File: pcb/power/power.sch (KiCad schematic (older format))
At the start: 28 parts, among them J1 Conn_Coaxial_Power, J2 GS3, SW1 SW_SPST, U1 L7805

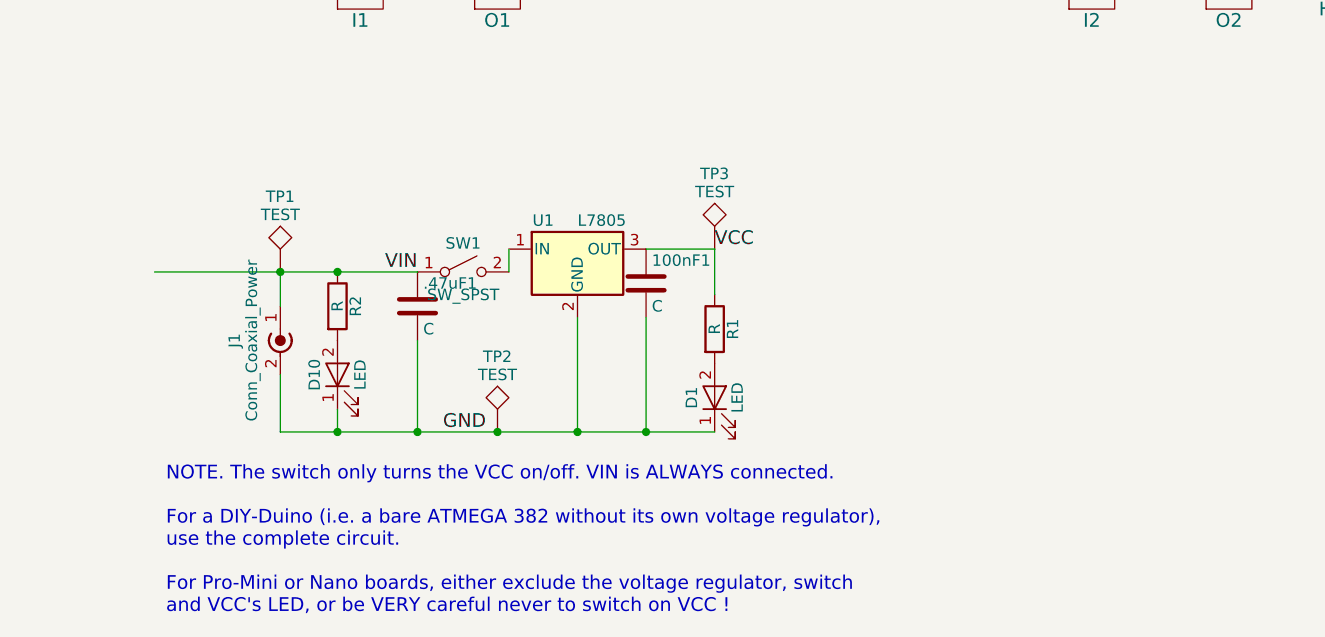
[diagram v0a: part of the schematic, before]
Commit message: Tidied up blank, and removed the voltage regulator from "power" module.
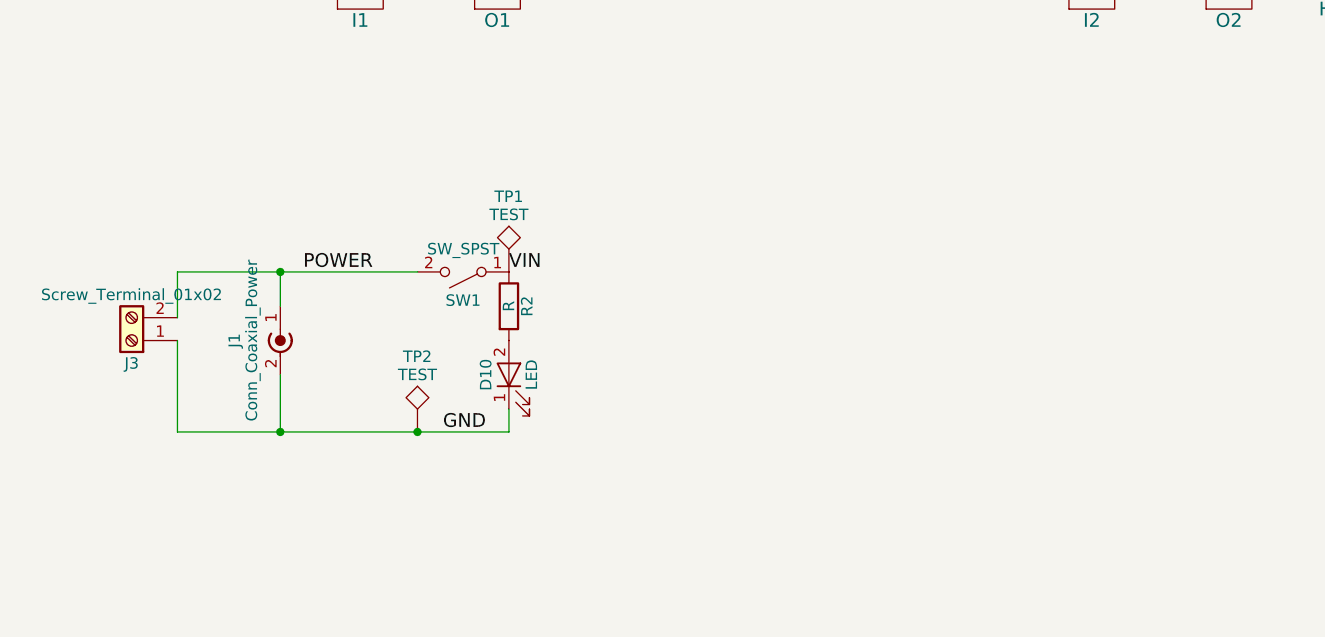
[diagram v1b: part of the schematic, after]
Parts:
- removed .47uF1, 100nF1: C, Capacitors_THT:CP_Radial_D6.3mm_P2.50mm, symbol C
- removed D1: LED, LEDs:LED_D3.0mm, symbol LED
- removed R1: R, Resistors_THT:R_Axial_DIN0204_L3.6mm_D1.6mm_P7.62mm_Horizontal, symbol R
- removed TP3: TEST, Connectors:PINTST, symbol TEST
- removed U1: L7805, Power_Integrations:TO-220, symbol L7805
- added J3: Screw_Terminal_01x02, Connectors_Terminal_Blocks:TerminalBlock_Philmore_TB132_02x5mm_Straight, symbol Screw_Terminal_01x02
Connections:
- net Earth: now also J3.1 (Pin_1)
- net VIN: no longer J1.1 (In)
- net POWER: now reaches SW1.2 (B)
- net POWER: now also J1.1 (In), J3.2 (Pin_2)
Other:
- note removed: "NOTE. The switch only turns the VCC on/off. VIN is ALWAYS connected.\n\nFor a DIY-Duino (i.e. a bare ATMEGA 382 without its own voltage regulator),\nuse the complete circuit.\n\nFor Pro-Mini or Nano boards, either exclude the voltage regulator, switch\nand VCC's LED, or be VERY careful never to switch on VCC !"
- moved on the sheet: D10, R2, SW1, TP1, TP2
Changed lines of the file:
@@
 	1    0    0    -1
 $EndComp
-$Comp
-L L7805 U1
-U 1 1 5AC3DA6D
-P 3050 4000
-F 0 "U1" H 2900 4125 50  0000 C CNN
-F 1 "L7805" H 3050 4125 50  0000 L CNN
-F 2 "Power_Integrations:TO-220" H 3075 3850 50  0001 L CIN
-F 3 "" H 3050 3950 50  0001 C CNN
-	1    3050 4000
-	1    0    0    -1
-$EndComp
-$Comp
-L C .47uF1
-U 1 1 5AC3DA90
-P 2350 4250
-F 0 ".47uF1" H 2375 4350 50  0000 L CNN
-F 1 "C" H 2375 4150 50  0000 L CNN
-F 2 "Capacitors_THT:CP_Radial_D6.3mm_P2.50mm" H 2388 4100 50  0001 C CNN
-F 3 "" H 2350 4250 50  0001 C CNN
-	1    2350 4250
-	1    0    0    -1
-$EndComp
-$Comp
-L C 100nF1
-U 1 1 5AC3DAAD
-P 3350 4150
-F 0 "100nF1" H 3375 4250 50  0000 L CNN
-F 1 "C" H 3375 4050 50  0000 L CNN
-F 2 "Capacitors_THT:CP_Radial_D6.3mm_P2.50mm" H 3388 4000 50  0001 C CNN
-F 3 "" H 3350 4150 50  0001 C CNN
-	1    3350 4150
-	1    0    0    -1
-$EndComp
-$Comp
-L R R1
-U 1 1 5AC3DACC
-P 3650 4350
-F 0 "R1" V 3730 4350 50  0000 C CNN
-F 1 "R" V 3650 4350 50  0000 C CNN
-F 2 "Resistors_THT:R_Axial_DIN0204_L3.6mm_D1.6mm_P7.62mm_Horizontal" V 3580 4350 50  0001 C CNN
-F 3 "" H 3650 4350 50  0001 C CNN
-	1    3650 4350
-	1    0    0    -1
-$EndComp
-$Comp
-L LED D1
-U 1 1 5AC3DC09
-P 3650 4650
-F 0 "D1" H 3650 4750 50  0000 C CNN
-F 1 "LED" H 3650 4550 50  0000 C CNN
-F 2 "LEDs:LED_D3.0mm" H 3650 4650 50  0001 C CNN
-F 3 "" H 3650 4650 50  0001 C CNN
-	1    3650 4650
-	0    -1   -1   0
-$EndComp
-Text Label 2350 4100 2    60   ~ 0
+Text Label 2750 4100 0    60   ~ 0
 VIN
-Text Label 3650 4000 0    60   ~ 0
-VCC
 $Comp
 L Conn_Coaxial_Power J1
@@
 L R R2
 U 1 1 5AC48099
-P 2000 4250
-F 0 "R2" V 2080 4250 50  0000 C CNN
-F 1 "R" V 2000 4250 50  0000 C CNN
-F 2 "Resistors_THT:R_Axial_DIN0204_L3.6mm_D1.6mm_P7.62mm_Horizontal" V 1930 4250 50  0001 C CNN
-F 3 "" H 2000 4250 50  0001 C CNN
-	1    2000 4250
+P 2750 4250
+F 0 "R2" V 2830 4250 50  0000 C CNN
+F 1 "R" V 2750 4250 50  0000 C CNN
+F 2 "Resistors_THT:R_Axial_DIN0204_L3.6mm_D1.6mm_P7.62mm_Horizontal" V 2680 4250 50  0001 C CNN
+F 3 "" H 2750 4250 50  0001 C CNN
+	1    2750 4250
 	1    0    0    -1
 $EndComp
@@
 L LED D10
 U 1 1 5AC480E4
-P 2000 4550
-F 0 "D10" H 2000 4650 50  0000 C CNN
-F 1 "LED" H 2000 4450 50  0000 C CNN
-F 2 "LEDs:LED_D3.0mm" H 2000 4550 50  0001 C CNN
-F 3 "" H 2000 4550 50  0001 C CNN
-	1    2000 4550
+P 2750 4550
+F 0 "D10" H 2750 4650 50  0000 C CNN
+F 1 "LED" H 2750 4450 50  0000 C CNN
+F 2 "LEDs:LED_D3.0mm" H 2750 4550 50  0001 C CNN
+F 3 "" H 2750 4550 50  0001 C CNN
+	1    2750 4550
 	0    -1   -1   0
 $EndComp
@@
 F 3 "" H 2550 4100 50  0001 C CNN
 	1    2550 4100
-	1    0    0    -1
+	-1   0    0    1
 $EndComp
 $Comp
 L TEST TP1
 U 1 1 5AC4A364
-P 1750 4100
-F 0 "TP1" H 1750 4400 50  0000 C BNN
-F 1 "TEST" H 1750 4350 50  0000 C CNN
-F 2 "Connectors:PINTST" H 1750 4100 50  0001 C CNN
-F 3 "" H 1750 4100 50  0001 C CNN
-	1    1750 4100
-	1    0    0    -1
-$EndComp
-$Comp
-L TEST TP3
-U 1 1 5AC4A405
-P 3650 4000
-F 0 "TP3" H 3650 4300 50  0000 C BNN
-F 1 "TEST" H 3650 4250 50  0000 C CNN
-F 2 "Connectors:PINTST" H 3650 4000 50  0001 C CNN
-F 3 "" H 3650 4000 50  0001 C CNN
-	1    3650 4000
+P 2750 4100
+F 0 "TP1" H 2750 4400 50  0000 C BNN
+F 1 "TEST" H 2750 4350 50  0000 C CNN
+F 2 "Connectors:PINTST" H 2750 4100 50  0001 C CNN
+F 3 "" H 2750 4100 50  0001 C CNN
+	1    2750 4100
 	1    0    0    -1
 $EndComp
@@
 L TEST TP2
 U 1 1 5AC4A450
-P 2700 4800
-F 0 "TP2" H 2700 5100 50  0000 C BNN
-F 1 "TEST" H 2700 5050 50  0000 C CNN
-F 2 "Connectors:PINTST" H 2700 4800 50  0001 C CNN
-F 3 "" H 2700 4800 50  0001 C CNN
-	1    2700 4800
+P 2350 4800
+F 0 "TP2" H 2350 5100 50  0000 C BNN
+F 1 "TEST" H 2350 5050 50  0000 C CNN
+F 2 "Connectors:PINTST" H 2350 4800 50  0001 C CNN
+F 3 "" H 2350 4800 50  0001 C CNN
+	1    2350 4800
 	1    0    0    -1
 $EndComp
@@
 Text Notes 6450 1850 0    60   ~ 0
 Use jumpers to enable each LED.
-Text Notes 1250 5600 0    60   ~ 0
-NOTE. The switch only turns the VCC on/off. VIN is ALWAYS connected.\n\nFor a DIY-Duino (i.e. a bare ATMEGA 382 without its own voltage regulator),\nuse the complete circuit.\n\nFor Pro-Mini or Nano boards, either exclude the voltage regulator, switch\nand VCC's LED, or be VERY careful never to switch on VCC !
-Wire Wire Line
-	2350 4400 2350 4800
 Wire Wire Line
 	6850 2150 7400 2150
@@
 Wire Wire Line
 	8000 3600 7700 3600
-Connection ~ 2000 4100
 Wire Wire Line
 	1750 4250 1750 4100
-Connection ~ 1750 4100
 Wire Wire Line
 	1750 4550 1750 4800
-Wire Wire Line
-	1200 4100 2350 4100
-Wire Wire Line
-	2000 4800 2000 4700
 Connection ~ 2350 4800
-Connection ~ 2000 4800
-Wire Wire Line
-	1750 4800 3650 4800
-Wire Wire Line
-	3350 4800 3350 4300
-Connection ~ 3350 4800
-Wire Wire Line
-	3650 4200 3650 4000
-Wire Wire Line
-	3650 4000 3350 4000
-Wire Wire Line
-	3050 4300 3050 4800
-Connection ~ 3050 4800
-Wire Wire Line
-	2750 4100 2750 4000
-Connection ~ 2700 4800
 $Comp
 L Output O2
@@
 Wire Wire Line
 	5600 2150 6050 2150
+Wire Wire Line
+	1300 4800 2750 4800
+Wire Wire Line
+	2750 4800 2750 4700
+Wire Wire Line
+	1300 4100 2350 4100
+Text Label 1850 4100 0    60   ~ 0
+POWER
+$Comp
+L Screw_Terminal_01x02 J3
+U 1 1 5AC4EAFB
+P 1100 4400
+F 0 "J3" H 1100 4500 50  0000 C CNN
+F 1 "Screw_Terminal_01x02" H 1100 4200 50  0000 C CNN
+F 2 "Connectors_Terminal_Blocks:TerminalBlock_Philmore_TB132_02x5mm_Straight" H 1100 4400 50  0001 C CNN
+F 3 "" H 1100 4400 50  0001 C CNN
+	1    1100 4400
+	-1   0    0    1
+$EndComp
+Wire Wire Line
+	1300 4300 1300 4100
+Connection ~ 1750 4100
+Wire Wire Line
+	1300 4400 1300 4800
+Connection ~ 1750 4800
 $EndSCHEMATC
